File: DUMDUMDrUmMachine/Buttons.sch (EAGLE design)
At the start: 42 parts

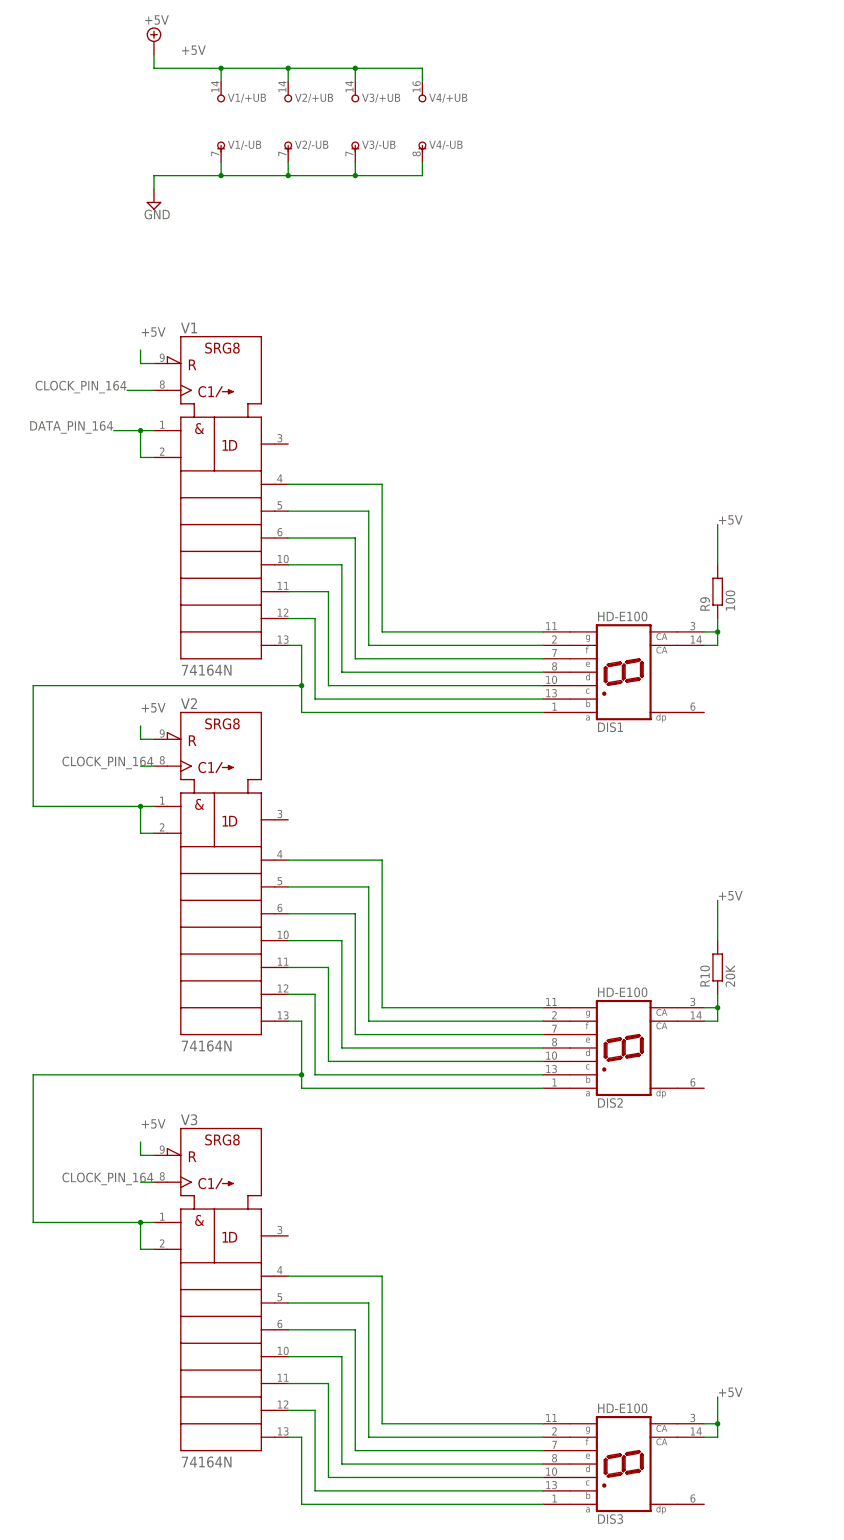
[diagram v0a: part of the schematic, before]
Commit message: separated display-pcb and button-pcb
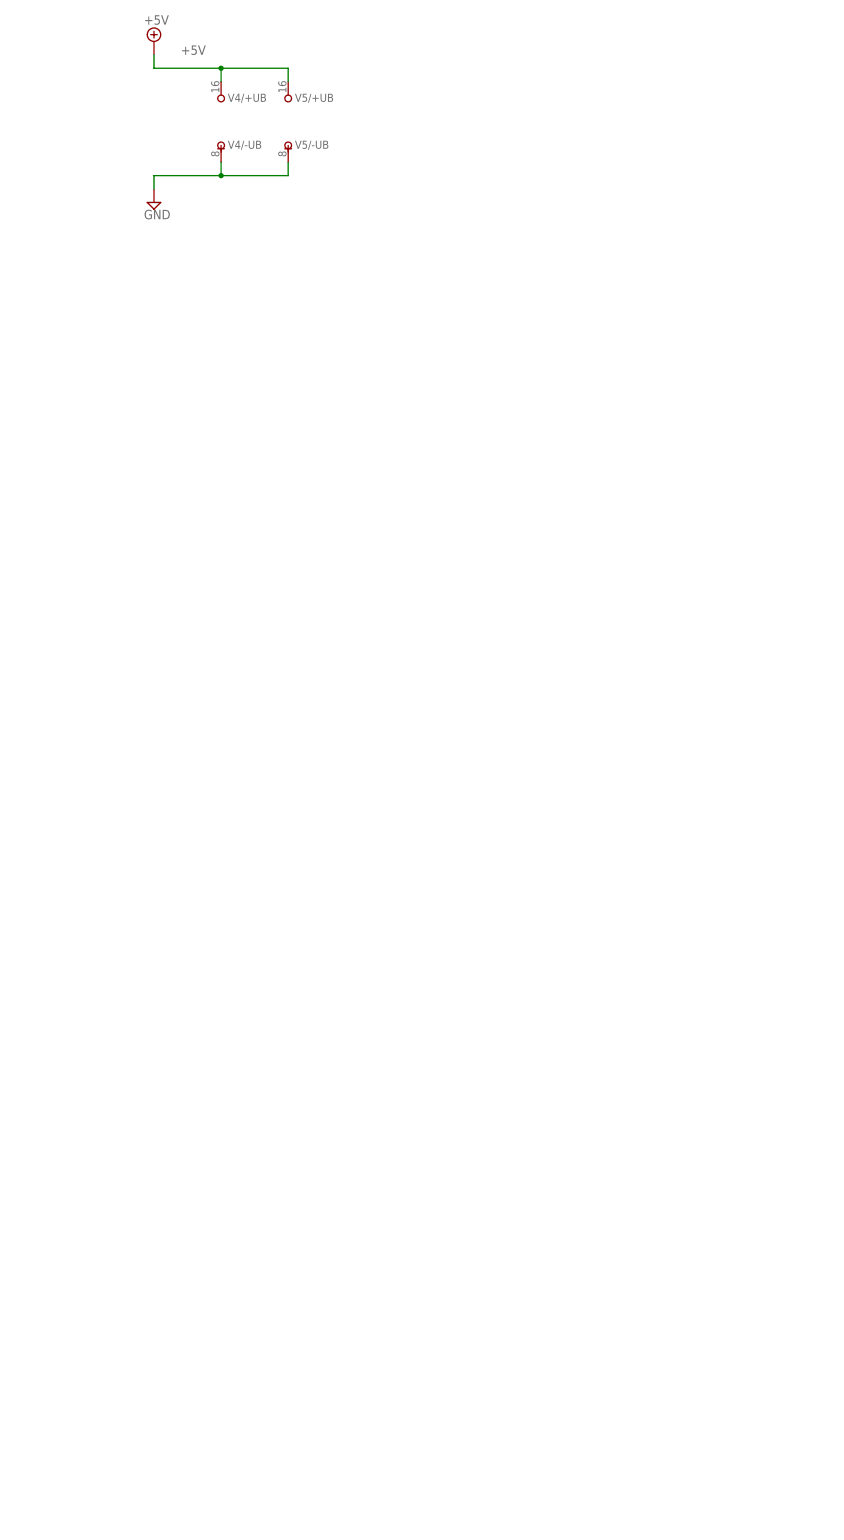
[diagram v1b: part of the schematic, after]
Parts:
- removed DIS1, DIS2, DIS3: HD-E100, display-hp:HD-E100
- removed R10: 20K, resistor:R-EU_0204/7
- removed R9: 100, resistor:R-EU_0204/7
- removed V1, V2, V3: 74164N, 74ttl-din:74164N
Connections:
- removed net CLOCK_PIN_164: V11.CLK, V21.CLK, V31.CLK
- removed net DATA_PIN_164: V11.A, V11.B
- removed net N$1: DIS2.A, V21.QH, V31.A, V31.B
- removed net N$10: DIS2.G, V21.QB
- removed net N$11: DIS2.F, V21.QC
- removed net N$12: DIS2.E, V21.QD
- removed net N$13: DIS2.D, V21.QE
- removed net N$14: DIS2.C, V21.QF
- removed net N$15: DIS2.B, V21.QG
- removed net N$16: DIS1.CA, DIS1.CA@1, R9.1
- removed net N$17: DIS3.F, V31.QC
- removed net N$18: DIS3.E, V31.QD
- removed net N$19: DIS3.D, V31.QE
- removed net N$2: DIS1.G, V11.QB
- removed net N$20: DIS3.C, V31.QF
- removed net N$21: DIS3.B, V31.QG
- removed net N$22: DIS3.A, V31.QH
- removed net N$23: DIS2.CA, DIS2.CA@1, R10.1
- removed net N$3: DIS1.F, V11.QC
- removed net N$4: DIS1.E, V11.QD
- removed net N$5: DIS1.D, V11.QE
- removed net N$6: DIS1.C, V11.QF
- removed net N$7: DIS1.B, V11.QG
- removed net N$8: DIS3.G, V31.QB
- removed net N$9: DIS1.A, V11.QH, V21.A, V21.B
- net +5V: now also V5/+UB.+UB; no longer DIS3.CA, DIS3.CA@1, R10.2, R9.2, V1/+UB.+UB, V11.!CLR, V2/+UB.+UB, V21.!CLR, V3/+UB.+UB, V31.!CLR
- net GND: now also V5/-UB.-UB; no longer V1/-UB.-UB, V2/-UB.-UB, V3/-UB.-UB
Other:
- moved on the sheet: V4/+UB, V4/-UB
